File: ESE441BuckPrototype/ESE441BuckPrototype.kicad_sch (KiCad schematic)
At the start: 0 parts

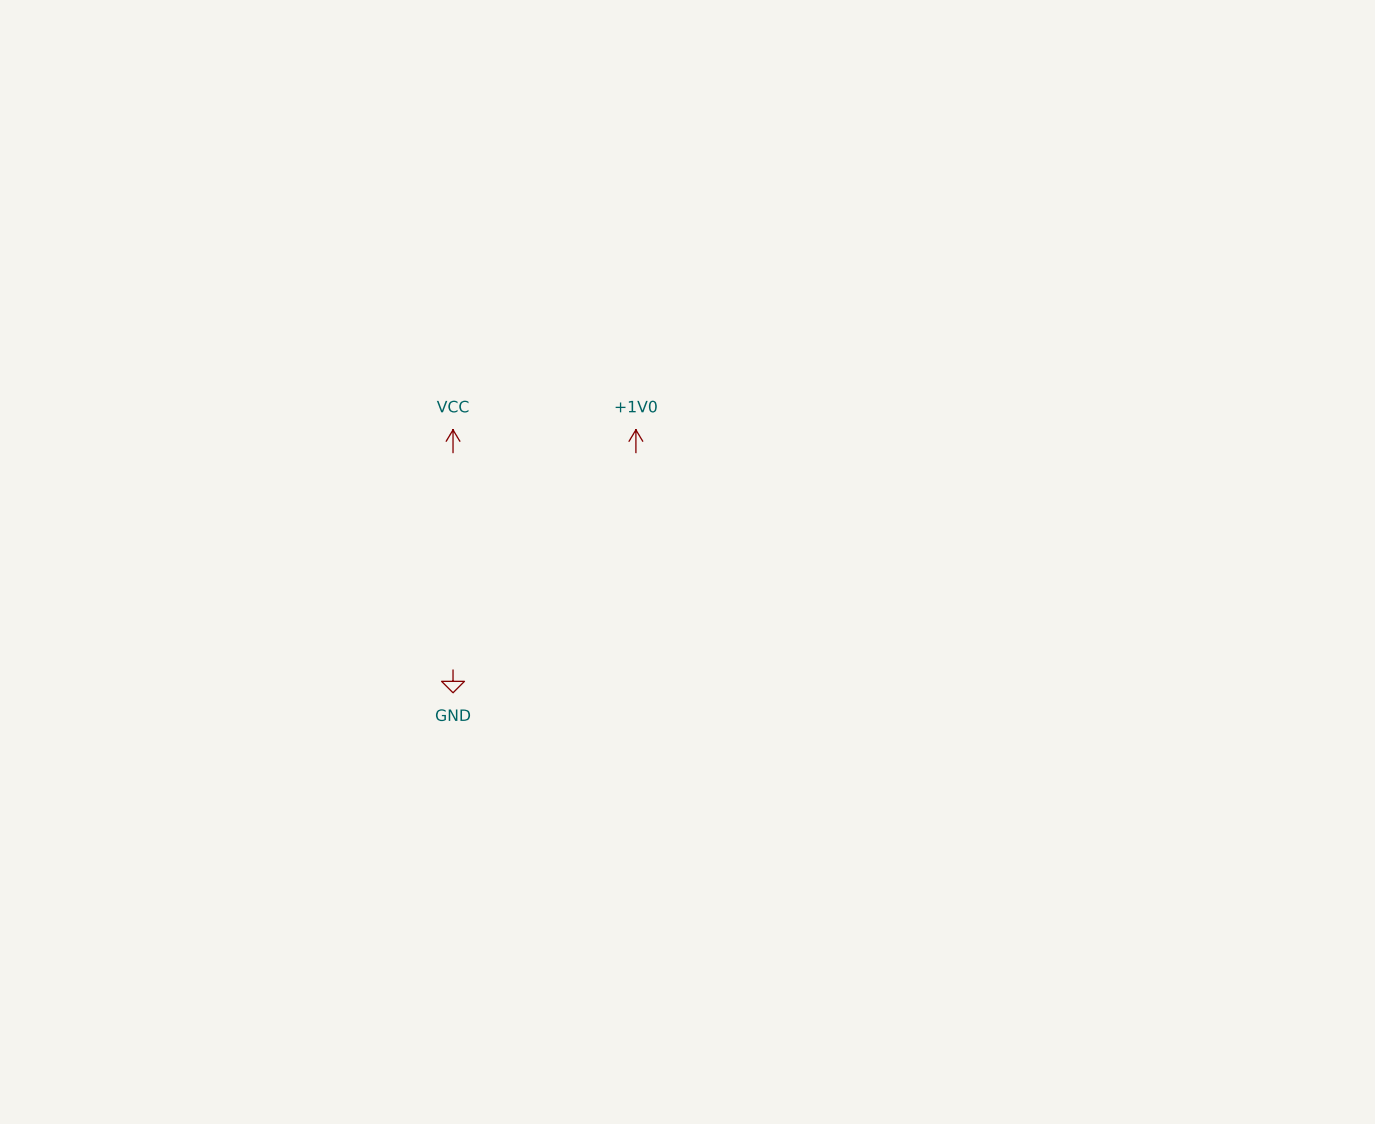
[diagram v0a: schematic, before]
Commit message: Add NCP81233MNTXG CAD files
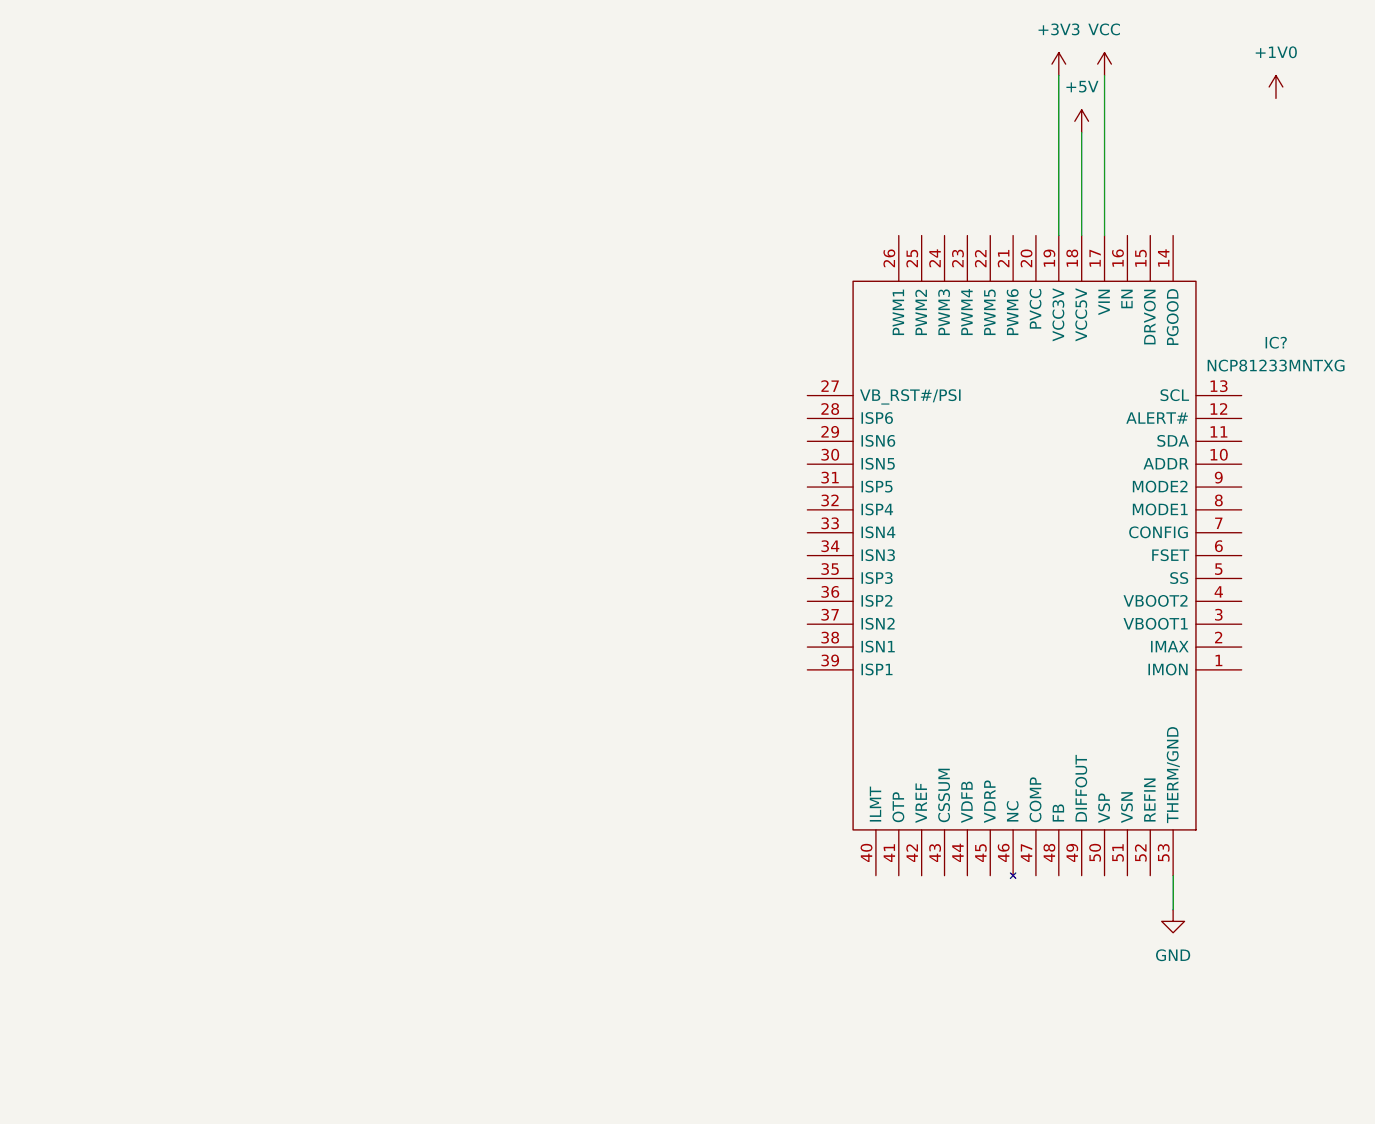
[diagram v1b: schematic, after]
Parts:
- added IC?: NCP81233MNTXG, QFN40P600X600X100-53N, symbol NCP81233MNTXG:NCP81233MNTXG
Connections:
- net GND: now also IC?.53 (THERM/GND)
- net VCC: now also IC?.17 (VIN)
- new net +3V3: IC?.19 (VCC3V)
- new net +5V: IC?.18 (VCC5V)
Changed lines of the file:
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@@
 (kicad_sch (version 20211123) (generator eeschema)
   (paper "A4")
-  (symbol (lib_id "power:VCC") (at 83.82 63.5 0) (unit 1)
+  (wire (pts (xy 151.13 21.59) (xy 151.13 39.37))
+    (stroke (width 0) (type default) (color 0 0 0 0))
+  )
+  (wire (pts (xy 156.21 39.37) (xy 156.21 21.59))
+    (stroke (width 0) (type default) (color 0 0 0 0))
+  )
+  (wire (pts (xy 153.67 27.94) (xy 153.67 39.37))
+    (stroke (width 0) (type default) (color 0 0 0 0))
+  )
+  (wire (pts (xy 163.83 110.49) (xy 163.83 114.3))
+    (stroke (width 0) (type default) (color 0 0 0 0))
+  )
+  (symbol (lib_id "power:VCC") (at 156.21 21.59 0) (unit 1)
     (in_bom yes) (on_board yes) (fields_autoplaced)
-    (property "Reference" "#PWR0102" (id 0) (at 83.82 67.31 0)
+    (property "Reference" "#PWR0102" (id 0) (at 156.21 25.4 0)
       (effects (font (size 1.27 1.27)) hide)
     )
-    (property "Value" "VCC" (id 1) (at 83.82 58.42 0))
-    (property "Footprint" "" (id 2) (at 83.82 63.5 0)
+    (property "Value" "VCC" (id 1) (at 156.21 16.51 0))
+    (property "Footprint" "" (id 2) (at 156.21 21.59 0)
       (effects (font (size 1.27 1.27)) hide)
     )
-    (property "Datasheet" "" (id 3) (at 83.82 63.5 0)
+    (property "Datasheet" "" (id 3) (at 156.21 21.59 0)
       (effects (font (size 1.27 1.27)) hide)
     )
     (pin "1")
   )
-  (symbol (lib_id "power:GND") (at 83.82 87.63 0) (unit 1)
+  (symbol (lib_id "power:GND") (at 163.83 114.3 0) (unit 1)
     (in_bom yes) (on_board yes) (fields_autoplaced)
-    (property "Reference" "#PWR0103" (id 0) (at 83.82 93.98 0)
+    (property "Reference" "#PWR0103" (id 0) (at 163.83 120.65 0)
       (effects (font (size 1.27 1.27)) hide)
     )
-    (property "Value" "GND" (id 1) (at 83.82 92.71 0))
-    (property "Footprint" "" (id 2) (at 83.82 87.63 0)
+    (property "Value" "GND" (id 1) (at 163.83 119.38 0))
+    (property "Footprint" "" (id 2) (at 163.83 114.3 0)
       (effects (font (size 1.27 1.27)) hide)
     )
-    (property "Datasheet" "" (id 3) (at 83.82 87.63 0)
+    (property "Datasheet" "" (id 3) (at 163.83 114.3 0)
       (effects (font (size 1.27 1.27)) hide)
     )
     (pin "1")
   )
-  (symbol (lib_id "power:+1V0") (at 104.14 63.5 0) (unit 1)
+  (symbol (lib_id "power:+1V0") (at 175.26 24.13 0) (unit 1)
     (in_bom yes) (on_board yes) (fields_autoplaced)
-    (property "Reference" "#PWR0101" (id 0) (at 104.14 67.31 0)
+    (property "Reference" "#PWR0101" (id 0) (at 175.26 27.94 0)
       (effects (font (size 1.27 1.27)) hide)
     )
-    (property "Value" "+1V0" (id 1) (at 104.14 58.42 0))
-    (property "Footprint" "" (id 2) (at 104.14 63.5 0)
+    (property "Value" "+1V0" (id 1) (at 175.26 19.05 0))
+    (property "Footprint" "" (id 2) (at 175.26 24.13 0)
       (effects (font (size 1.27 1.27)) hide)
     )
-    (property "Datasheet" "" (id 3) (at 104.14 63.5 0)
+    (property "Datasheet" "" (id 3) (at 175.26 24.13 0)
       (effects (font (size 1.27 1.27)) hide)
     )
     (pin "1")
+  )
+  (symbol (lib_id "power:+3V3") (at 151.13 21.59 0) (unit 1)
+    (in_bom yes) (on_board yes) (fields_autoplaced)
+    (property "Reference" "#PWR?" (id 0) (at 151.13 25.4 0)
+      (effects (font (size 1.27 1.27)) hide)
+    )
+    (property "Value" "+3V3" (id 1) (at 151.13 16.51 0))
+    (property "Footprint" "" (id 2) (at 151.13 21.59 0)
+      (effects (font (size 1.27 1.27)) hide)
+    )
+    (property "Datasheet" "" (id 3) (at 151.13 21.59 0)
+      (effects (font (size 1.27 1.27)) hide)
+    )
+    (pin "1")
+  )
+  (symbol (lib_id "power:+5V") (at 153.67 27.94 0) (unit 1)
+    (in_bom yes) (on_board yes) (fields_autoplaced)
+    (property "Reference" "#PWR?" (id 0) (at 153.67 31.75 0)
+      (effects (font (size 1.27 1.27)) hide)
+    )
+    (property "Value" "+5V" (id 1) (at 153.67 22.86 0))
+    (property "Footprint" "" (id 2) (at 153.67 27.94 0)
+      (effects (font (size 1.27 1.27)) hide)
+    )
+    (property "Datasheet" "" (id 3) (at 153.67 27.94 0)
+      (effects (font (size 1.27 1.27)) hide)
+    )
+    (pin "1")
+  )
+  (symbol (lib_id "NCP81233MNTXG:NCP81233MNTXG") (at 171.45 87.63 180) (unit 1)
+    (in_bom yes) (on_board yes) (fields_autoplaced)
+    (property "Reference" "IC?" (id 0) (at 175.26 51.3205 0))
+    (property "Value" "NCP81233MNTXG" (id 1) (at 175.26 53.8605 0))
+    (property "Footprint" "QFN40P600X600X100-53N" (id 2) (at 127 105.41 0)
+      (effects (font (size 1.27 1.27)) (justify left) hide)
+    )
+    (property "Datasheet" "http://www.onsemi.com/pub/Collateral/NCP81233-D.PDF" (id 3) (at 127 102.87 0)
+      (effects (font (size 1.27 1.27)) (justify left) hide)
+    )
+    (property "Description" "Multi-Phase Controller, Configurable, 4.5 V to 20 V, I2C" (id 4) (at 127 100.33 0)
+      (effects (font (size 1.27 1.27)) (justify left) hide)
+    )
+    (property "Height" "1" (id 5) (at 127 97.79 0)
+      (effects (font (size 1.27 1.27)) (justify left) hide)
+    )
+    (property "Mouser Part Number" "863-NCP81233MNTXG" (id 6) (at 127 95.25 0)
+      (effects (font (size 1.27 1.27)) (justify left) hide)
+    )
+    (property "Mouser Price/Stock" "https://www.mouser.co.uk/ProductDetail/ON-Semiconductor/NCP81233MNTXG/?qs=z6PAvqrnkvQJZ4opJwgsbQ%3D%3D" (id 7) (at 127 92.71 0)
+      (effects (font (size 1.27 1.27)) (justify left) hide)
+    )
+    (property "Manufacturer_Name" "onsemi" (id 8) (at 127 90.17 0)
+      (effects (font (size 1.27 1.27)) (justify left) hide)
+    )
+    (property "Manufacturer_Part_Number" "NCP81233MNTXG" (id 9) (at 127 87.63 0)
+      (effects (font (size 1.27 1.27)) (justify left) hide)
+    )
+    (pin "1")
+    (pin "10")
+    (pin "11")
+    (pin "12")
+    (pin "13")
+    (pin "14")
+    (pin "15")
+    (pin "16")
+    (pin "17")
+    (pin "18")
+    (pin "19")
+    (pin "2")
+    (pin "20")
+    (pin "21")
+    (pin "22")
+    (pin "23")
+    (pin "24")
+    (pin "25")
+    (pin "26")
+    (pin "27")
+    (pin "28")
+    (pin "29")
+    (pin "3")
+    (pin "30")
+    (pin "31")
+    (pin "32")
+    (pin "33")
+    (pin "34")
+    (pin "35")
+    (pin "36")
+    (pin "37")
+    (pin "38")
+    (pin "39")
+    (pin "4")
+    (pin "40")
+    (pin "41")
+    (pin "42")
+    (pin "43")
+    (pin "44")
+    (pin "45")
+    (pin "46")
+    (pin "47")
+    (pin "48")
+    (pin "49")
+    (pin "5")
+    (pin "50")
+    (pin "51")
+    (pin "52")
+    (pin "53")
+    (pin "6")
+    (pin "7")
+    (pin "8")
+    (pin "9")
   )
   (sheet_instances
@@
       (reference "#PWR0103") (unit 1) (value "GND") (footprint "")
     )
+    (path "/a6f96da5-2bd6-4f19-8f06-ef05219a590f"
+      (reference "#PWR?") (unit 1) (value "+3V3") (footprint "")
+    )
+    (path "/c8b8da4d-109b-4aaa-a3a0-cf188926c81b"
+      (reference "#PWR?") (unit 1) (value "+5V") (footprint "")
+    )
+    (path "/ca983285-b6ff-4c2f-aafc-af5881120528"
+      (reference "IC?") (unit 1) (value "NCP81233MNTXG") (footprint "QFN40P600X600X100-53N")
+    )
   )

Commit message: Add basic hierarchical sheets
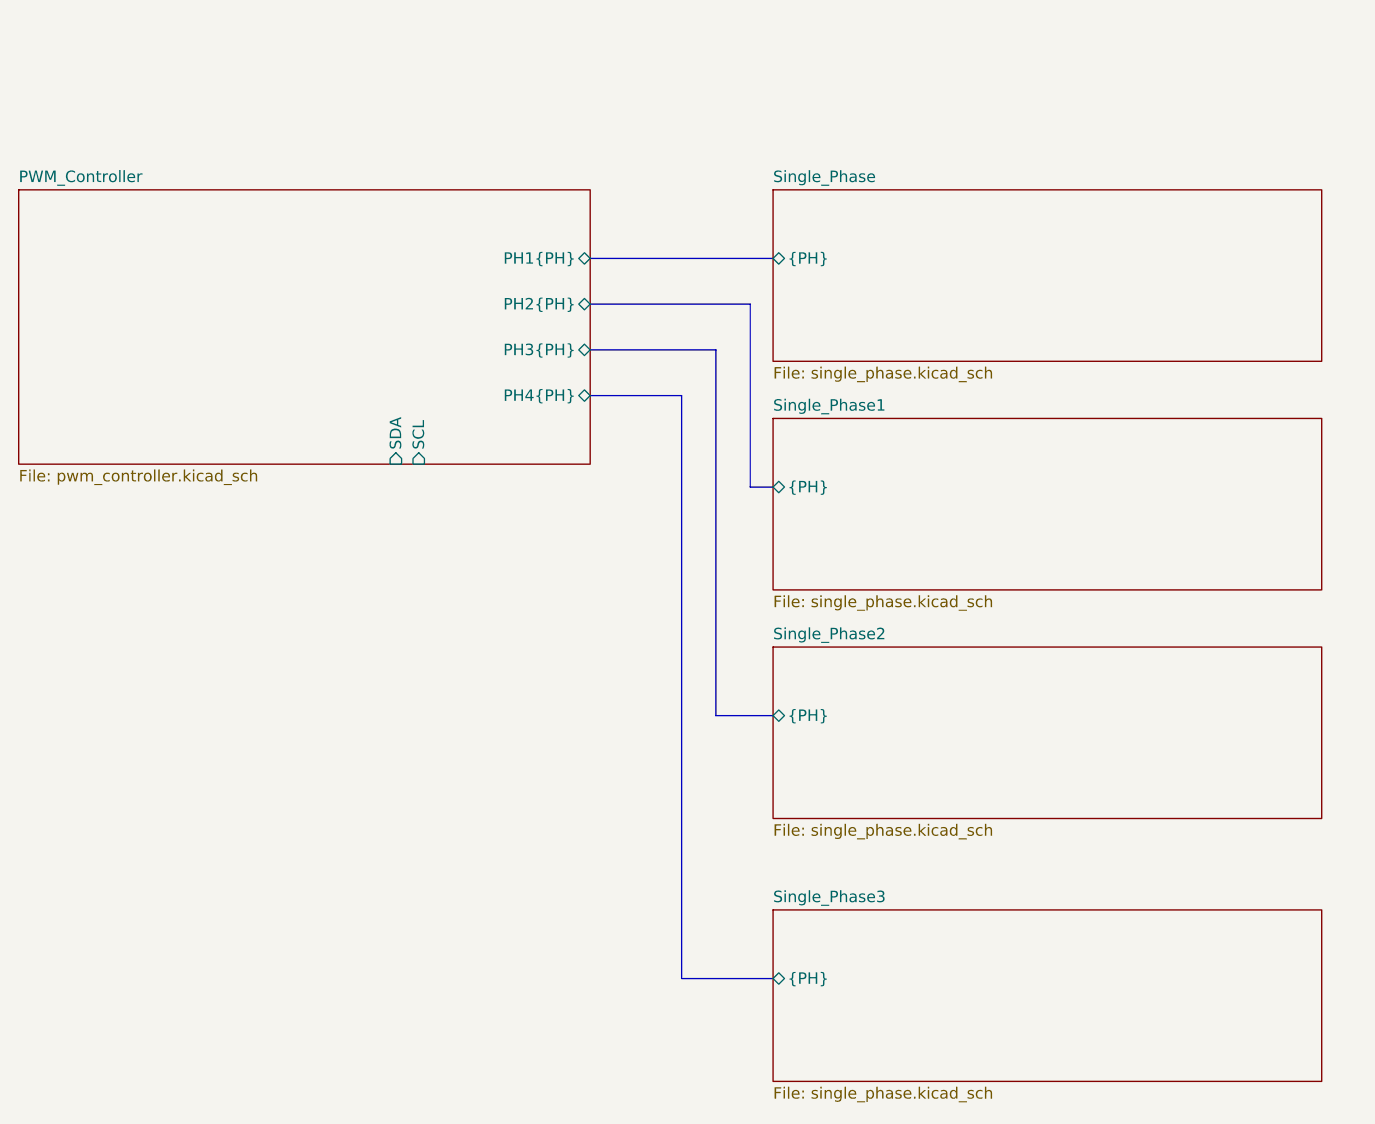
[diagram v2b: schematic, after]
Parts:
- removed IC?: NCP81233MNTXG, QFN40P600X600X100-53N, symbol NCP81233MNTXG:NCP81233MNTXG
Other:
- added sheet PWM_Controller (pwm_controller.kicad_sch)
- added sheet Single_Phase (single_phase.kicad_sch)
- added sheet Single_Phase1 (single_phase.kicad_sch)
- added sheet Single_Phase2 (single_phase.kicad_sch)
- added sheet Single_Phase3 (single_phase.kicad_sch)
